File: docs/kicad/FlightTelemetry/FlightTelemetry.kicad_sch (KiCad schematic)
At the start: 11 parts, among them J1 BMP388, J2 NEO-M9N, J3 Micro SD, J4 INA219, J5 MP1584 (5V), J6 +3.3V_BUS, J7 Active Buzzer, J8 DS18B20-Ext. Thermometer, U1 ESP32 DevKitC V4

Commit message: Sprint 13a - DS18B20 external thermometer integrated (serial output)
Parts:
- removed R1: 10K, symbol Device:R

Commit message: correct power supply in schematic and physical considerations
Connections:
- net IN+ / MP1584: no longer BT1.1 (+)
- new net VIN+ / INA219: BT1.1 (+)
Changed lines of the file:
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@@
 		(comment 7 "CS, SDO and INT left unconnected")
 	)
-	(junction
-		(at 34.29 54.61)
-		(diameter 0)
-		(color 0 0 0 0)
-	)
 	(wire
 		(pts
@@
 	(wire
 		(pts
-			(xy 34.29 54.61) (xy 34.29 58.42)
+			(xy 34.29 50.8) (xy 34.29 58.42)
 		)
 		(stroke
@@
 	(wire
 		(pts
-			(xy 34.29 54.61) (xy 38.1 54.61)
-		)
-		(stroke
-			(width 0)
-			(type default)
-		)
-	)
-	(wire
-		(pts
 			(xy 210.82 57.15) (xy 220.98 57.15)
 		)
@@
 		(pts
 			(xy 214.63 95.25) (xy 220.98 95.25)
-		)
-		(stroke
-			(width 0)
-			(type default)
-		)
-	)
-	(wire
-		(pts
-			(xy 34.29 50.8) (xy 34.29 54.61)
 		)
 		(stroke
@@
 		)
 	)
-	(global_label "IN+ {slash} MP1584"
-		(shape input)
-		(at 38.1 54.61 0)
-		(fields_autoplaced yes)
-		(effects
-			(font
-				(size 1.27 1.27)
-			)
-			(justify left)
-		)
-		(property "Intersheetrefs" "${INTERSHEET_REFS}"
-			(at 55.418 54.61 0)
-			(hide yes)
-			(show_name no)
-			(do_not_autoplace no)
-			(effects
-				(font
-					(size 1.27 1.27)
-				)
-				(justify left)
-			)
-		)
-	)

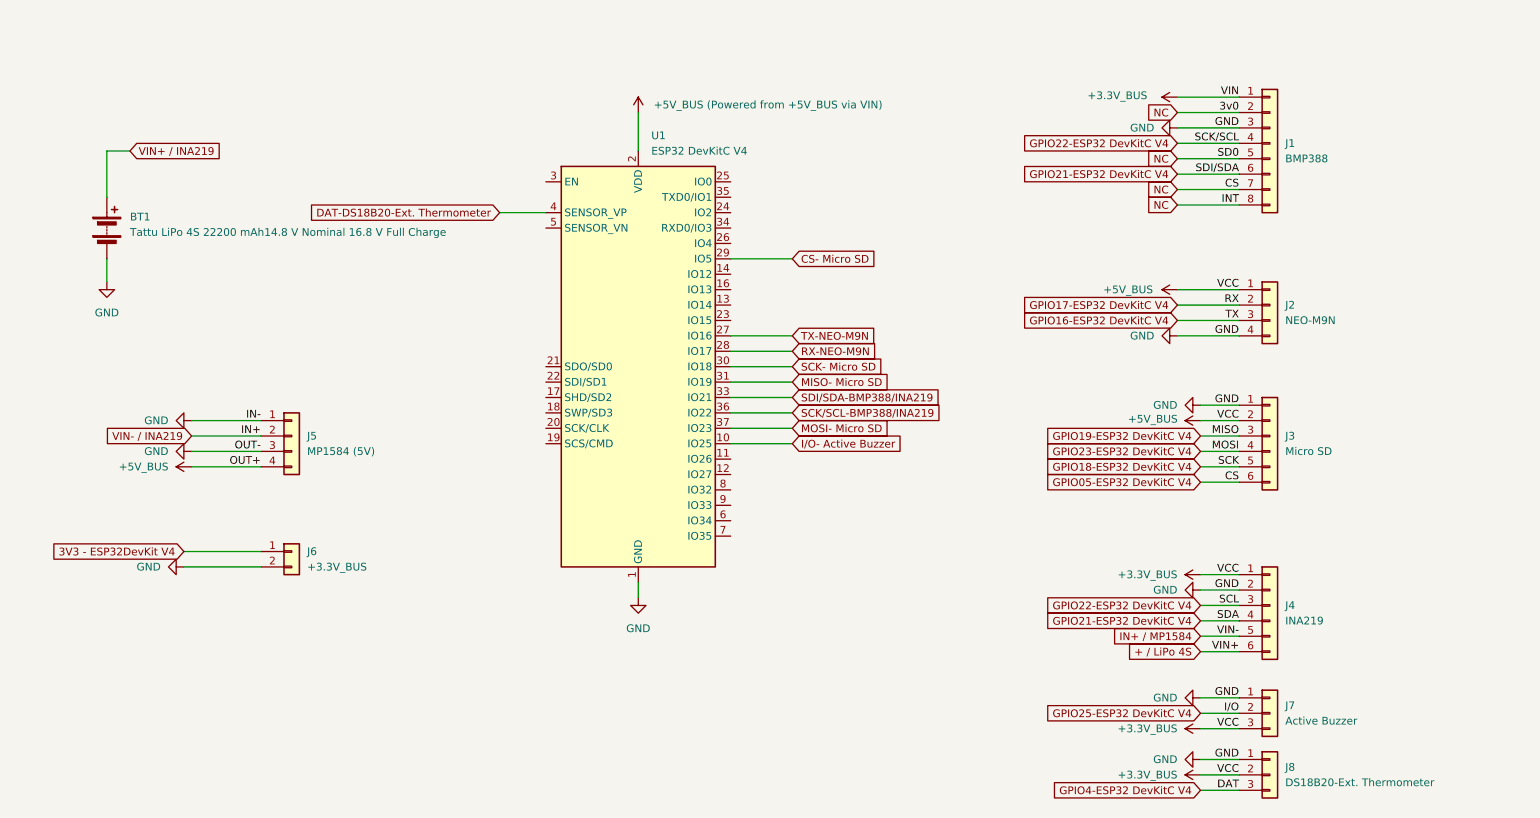
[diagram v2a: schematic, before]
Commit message: docs: update Mk1 baseline and add Power Deck v0.1
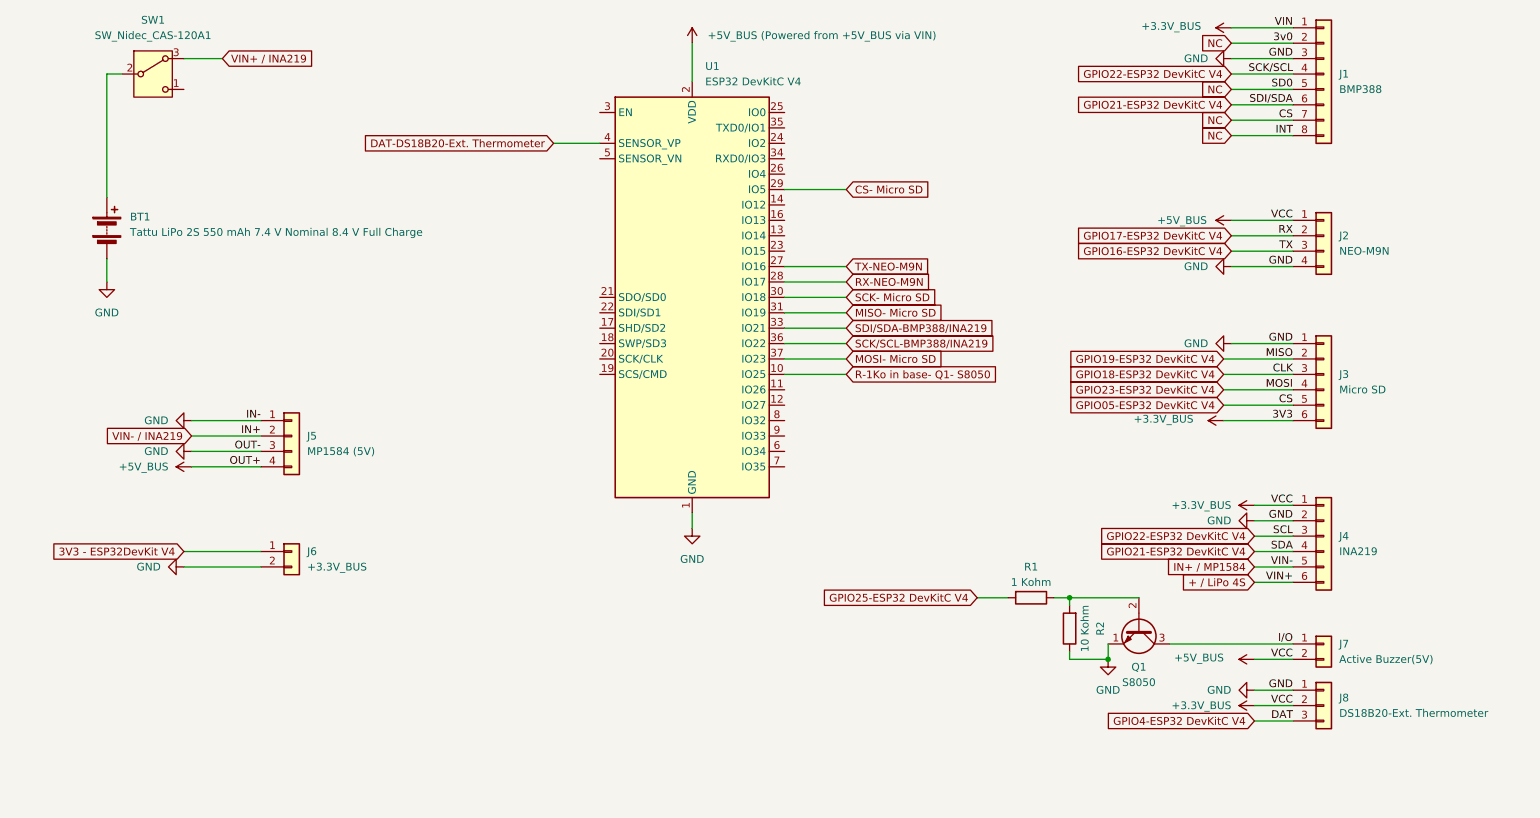
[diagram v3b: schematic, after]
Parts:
- removed J7: Active Buzzer, symbol Connector_Generic:Conn_01x03
- added J7: Active Buzzer(5V), symbol Connector_Generic:Conn_01x02
- added Q1: S8050, Package_TO_SOT_THT:TO-92_Inline, symbol Transistor_BJT:S8050
- added R1: 1 Kohm, symbol Device:R
- added R2: 10 Kohm, symbol Device:R
- added SW1: SW_Nidec_CAS-120A1, Button_Switch_SMD:Nidec_Copal_CAS-120A, symbol Switch:SW_Nidec_CAS-120A1
- BT1: value Tattu LiPo 4S 22200 mAh14.8 V Nominal 16.8 V Full Charge -> Tattu LiPo 2S 550 mAh 7.4 V Nominal 8.4 V Full Charge
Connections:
- net +3.3V_BUS: now also J3.6 (Pin_6), J7.2 (Pin_2); no longer J3.2 (Pin_2)
- net GND: now also Q1.1 (E), R2.1
- net GPIO05-ESP32 DevKitC V4: now also J3.5 (Pin_5); no longer J3.6 (Pin_6)
- net GPIO18-ESP32 DevKitC V4: now also J3.3 (Pin_3); no longer J3.5 (Pin_5)
- net GPIO19-ESP32 DevKitC V4: now also J3.2 (Pin_2); no longer J3.3 (Pin_3)
- net GPIO25-ESP32 DevKitC V4: now also R1.2
- net VIN+ / INA219: now also SW1.3 (A); no longer BT1.1 (+)
- net I/O- Active Buzzer renamed R-1Ko in base- Q1- S8050
- new net: Q1.2 (B), R1.1, R2.2
- new net: BT1.1 (+), SW1.2 (B)
- new net I/O: J7.1 (Pin_1), Q1.3 (C)
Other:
- moved on the sheet: J1, J2, J4, J8, U1

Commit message: chore: rename project to RocketOS
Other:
- title: Flight Telemetry & Data Logger -> RocketOS
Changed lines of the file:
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@@
 	(paper "A4")
 	(title_block
-		(title "Flight Telemetry & Data Logger")
+		(title "RocketOS")
 		(rev "v0.14.0")
 		(comment 1 "INA219 / MP1584 / Tattu LiPo2S 550 mAh")
